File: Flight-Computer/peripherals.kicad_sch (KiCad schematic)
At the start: 36 parts, among them P10 Micro_SD_Card, P9 1984659, Q5 QS5U17TR, Q6 QS5U17TR, U10 TS391IYLT, U11 TS391IYLT, U6 SST25VF040B-50-4I-S2AE-T, U7 RFM95W-868S2, U8 CP2102-GMR(QFN28), U9 TS391IYLT

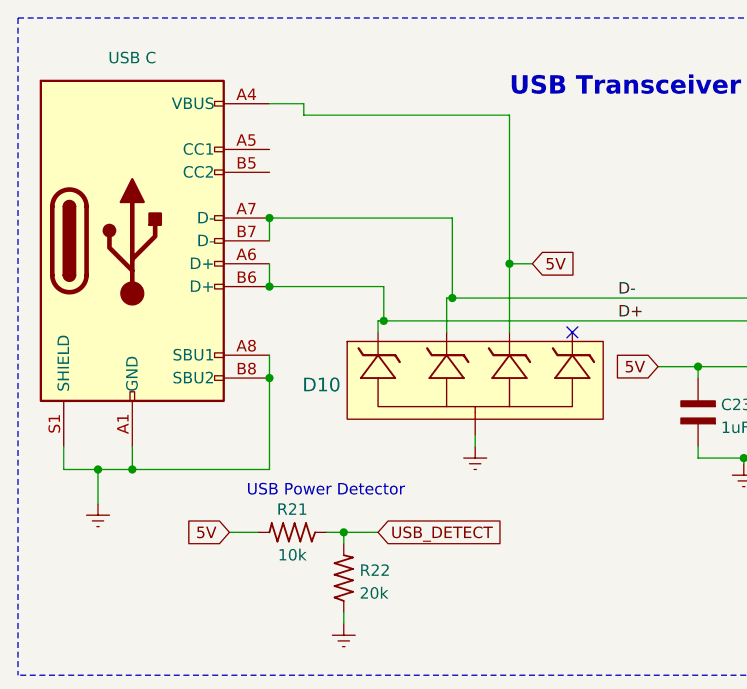
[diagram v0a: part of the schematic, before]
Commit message: SPI Flash Daisy chain
need to review and likely rewire the daisy chain
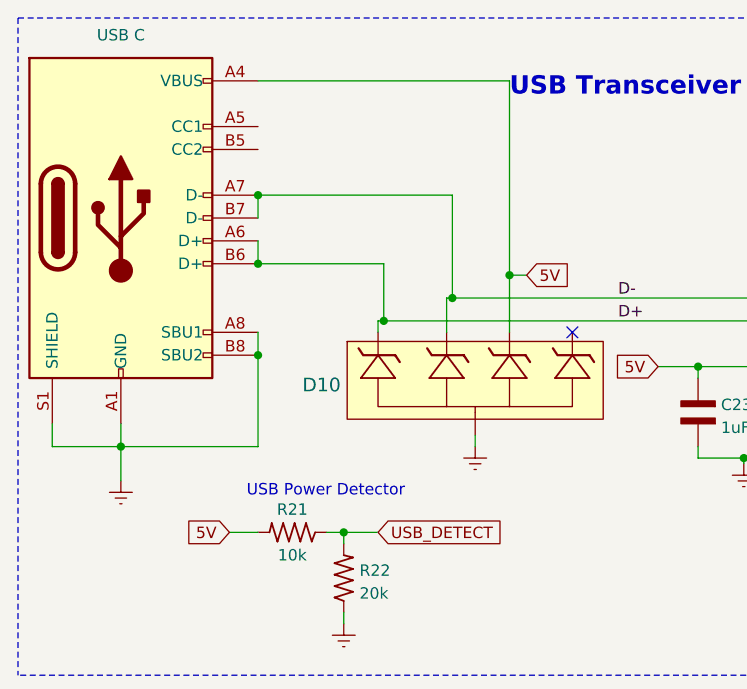
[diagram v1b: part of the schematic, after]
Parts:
- removed J: USB C, symbol Connector:USB_C_Receptacle_USB2.0_16P
- added J6: USB C, symbol Connector:USB_C_Receptacle_USB2.0_16P
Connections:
- net 5V: now also J6.A4 (VBUS), J6.A9 (VBUS), J6.B4 (VBUS), J6.B9 (VBUS)
- net D+: now also J6.A6 (D+), J6.B6 (D+)
- net D-: now also J6.A7 (D-), J6.B7 (D-)
- net Earth: now also J6.A1 (GND), J6.A12 (GND), J6.A8 (SBU1), J6.B1 (GND), J6.B12 (GND), J6.B8 (SBU2), J6.S1 (SHIELD)
